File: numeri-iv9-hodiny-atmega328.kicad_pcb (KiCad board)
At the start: 2 copper layers, 160 x 50 mm, 64 parts, among them J2 Screw_Terminal_01x04, J3 USB-C, J4 PINHD_1x3_Female, J5 HW-084, Q1 BC557, Q2 BC557, SW1 RESET, SW2 Horizontal, SW3 Vertical, U1 ATmega328-P, U2 TPIC6B595N, U3 TPIC6B595N, U4 TPIC6B595N, U5 TPIC6B595N, Y1 6MHz

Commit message: preventívne
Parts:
- removed R17: 550R, Resistor_THT:R_Axial_DIN0207_L6.3mm_D2.5mm_P10.16mm_Horizontal
- added G***: LOGO, LOGO, F.Cu at (93.5, 75.8)
- added G***: LOGO, LOGO, F.Cu at (84.5, 93.2)
- added R4: 1K, Potentiometer_THT:Potentiometer_Bourns_3296W_Vertical, F.Cu at (200.0, 117.8)
- added REF**: JUP_P14mm, PCM_SL_Jumpers:JUP_P14mm, F.Cu at (211.8, 111.8)
- added REF**: JUP_P14mm, PCM_SL_Jumpers:JUP_P14mm, F.Cu at (130.2, 111.0)
- added REF**: JUP_P14mm, PCM_SL_Jumpers:JUP_P14mm, F.Cu at (157.8, 111.0)
- C12, C13, C14, C16, C3, C4, C5, C6, C7: footprint Capacitor_THT:C_Disc_D3.0mm_W2.0mm_P2.50mm -> Capacitor_THT:C_Disc_D6.0mm_W2.5mm_P5.00mm
- J4: footprint Connector_PinSocket_2.54mm:PinSocket_1x03_P2.54mm_Vertical -> Connector_PinHeader_2.54mm:PinHeader_1x03_P2.54mm_Vertical
- R1: footprint Resistor_THT:R_Axial_DIN0207_L6.3mm_D2.5mm_P10.16mm_Horizontal -> Resistor_THT:R_Axial_DIN0207_L6.3mm_D2.5mm_P5.08mm_Vertical; moved to B.Cu
- R11, R12, R6, R7, R9: footprint Resistor_THT:R_Axial_DIN0207_L6.3mm_D2.5mm_P10.16mm_Horizontal -> Resistor_THT:R_Axial_DIN0207_L6.3mm_D2.5mm_P15.24mm_Horizontal
- R13, R16: footprint Resistor_THT:R_Axial_DIN0207_L6.3mm_D2.5mm_P10.16mm_Horizontal -> Resistor_THT:R_Axial_DIN0207_L6.3mm_D2.5mm_P5.08mm_Vertical
- R15: footprint Resistor_THT:R_Axial_DIN0414_L11.9mm_D4.5mm_P15.24mm_Horizontal -> Resistor_THT:R_Axial_DIN0414_L11.9mm_D4.5mm_P25.40mm_Horizontal
- R8: footprint Resistor_THT:R_Axial_DIN0207_L6.3mm_D2.5mm_P2.54mm_Vertical -> Resistor_THT:R_Axial_DIN0207_L6.3mm_D2.5mm_P10.16mm_Horizontal
- SERIAL1: footprint Connector_PinHeader_2.54mm:PinHeader_1x02_P2.54mm_Vertical -> Connector_PinSocket_2.54mm:PinSocket_1x02_P2.54mm_Vertical
- SW2, SW3: footprint TerminalBlock_Phoenix:TerminalBlock_Phoenix_MPT-0,5-2-2.54_1x02_P2.54mm_Horizontal -> TerminalBlock_Phoenix:TerminalBlock_Phoenix_MPT-0,5-2-2.54_1x02_P2.54mm_Horizontal_RAW
- U2, U3, U4, U5: footprint Package_DIP:DIP-20_W7.62mm_Socket -> Package_DIP:DIP-20_W7.62mm_Socket_With_IC
- moved R5 65.2 mm to (125.7, 118.0), turned to 180 degrees
- moved D2 43.3 mm to (95.9, 103.2)
- moved R13 42.1 mm to (195.5, 117.8), turned to 90 degrees
- moved D1 28.1 mm to (161.7, 118.5), turned to 180 degrees
- moved R15 26.7 mm to (144.0, 99.4), turned to 90 degrees
- moved R16 22.4 mm to (189.8, 111.5), turned to 180 degrees
- moved Q2 20.0 mm to (187.0, 117.8), turned to 90 degrees
- moved C6 19.1 mm to (167.5, 84.1), turned to 90 degrees
- moved J4 19.1 mm to (115.5, 114.5), turned to -90 degrees
- moved TSV2 16.6 mm to (92.5, 92.2)
- moved TSV1 16.0 mm to (100.0, 92.5)
- moved RV2 12.1 mm to (90.2, 107.5)
- moved R14 11.8 mm to (172.7, 117.8)
- moved C7 9.29 mm to (149.5, 83.0)
- moved Q1 8.61 mm to (191.1, 115.2), turned to -90 degrees
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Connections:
- J4 pad 1: +3.3V -> +3V3
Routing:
- net +5V/+3V3: track 100.7 -> 9.05 mm
- net VBTN: track 13.7 -> 95.6 mm
- net +5V_DEC: track 28.8 -> 101.5 mm
- net MISO/HBTN: track 0.00 -> 66.4 mm
- net DEC_OUT: track 0.00 -> 34.6 mm
- net PB2: track 12.4 -> 43.0 mm
- net +3V3: track 0.00 -> 23.2 mm
- net +5V: track 169.7 -> 189.1 mm
- net ~{G}~: track 65.6 -> 47.5 mm
- net ~{PON}: track 9.34 -> 26.6 mm
- net Net-(U1-PC0): track 0.00 -> 9.25 mm
- net Net-(U1-XTAL2/PB7): track 8.24 -> 0.00 mm
- net Net-(U1-XTAL1/PB6): track 8.12 -> 0.00 mm
- net RX: track 0.00 -> 5.99 mm
- net Net-(Q2-E): track 0.00 -> 4.92 mm
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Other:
- board text added: "+5V VCC +3V3"

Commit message: preventívne
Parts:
- removed the REF** at (157.8, 111.0)
- added R10: 619R, Resistor_THT:R_Axial_DIN0207_L6.3mm_D2.5mm_P7.62mm_Horizontal, F.Cu at (248.2, 86.9)
- added R17: 464R, Resistor_THT:R_Axial_DIN0207_L6.3mm_D2.5mm_P2.54mm_Vertical, F.Cu at (192.0, 104.5)
- added R17: 464R, Resistor_THT:R_Axial_DIN0207_L6.3mm_D2.5mm_P2.54mm_Vertical, F.Cu at (198.0, 104.5)
- added R17: 464R, Resistor_THT:R_Axial_DIN0207_L6.3mm_D2.5mm_P2.54mm_Vertical, F.Cu at (195.0, 104.5)
- added R18: 464R, Resistor_THT:R_Axial_DIN0207_L6.3mm_D2.5mm_P7.62mm_Horizontal, B.Cu at (199.2, 96.2)
- added R19: 330R, Resistor_THT:R_Axial_DIN0207_L6.3mm_D2.5mm_P7.62mm_Horizontal, F.Cu at (245.8, 95.5)
- R16: footprint Resistor_THT:R_Axial_DIN0207_L6.3mm_D2.5mm_P5.08mm_Vertical -> Resistor_THT:R_Axial_DIN0207_L6.3mm_D2.5mm_P10.16mm_Horizontal
- moved R16 7.83 mm to (182.8, 115.0)
- moved RGB_LED1 4.78 mm to (186.5, 110.0)
- moved D1 2.09 mm to (163.3, 117.2)
- moved C12 0.72 mm to (182.5, 112.0)
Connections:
- RGB_LED1 pad 2: LED_R -> Net-(RGB_LED1-RA)
- RGB_LED1 pad 3: LED_G -> Net-(RGB_LED1-GA)
- RGB_LED1 pad 4: LED_B -> Net-(RGB_LED1-BA)
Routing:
- net PB2: track 43.0 -> 35.8 mm
- net LED_R: track 6.99 -> 0.16 mm
- net LED_G: track 6.99 -> 0.16 mm
- net LED_B: track 6.99 -> 0.16 mm
- net Net-(RGB_LED1-BA): track 0.00 -> 5.59 mm
- net Net-(Q1-B): track 0.00 -> 4.68 mm
- net unconnected-(U1-(PWM)PD5-Pad11): track 3.81 -> 7.19 mm
- net ~{PON}: track 26.6 -> 28.8 mm

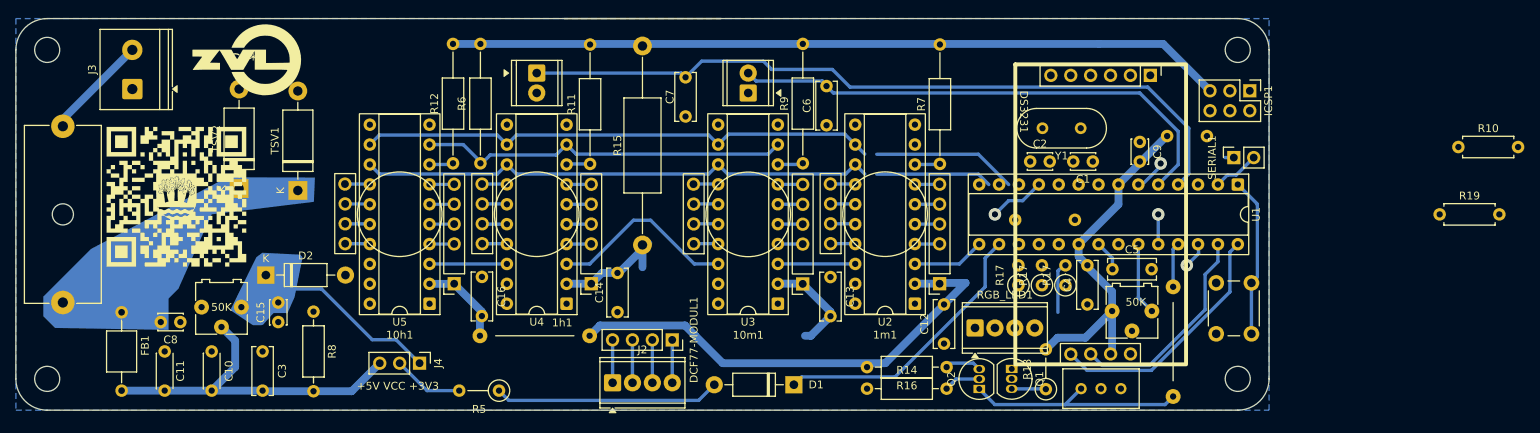
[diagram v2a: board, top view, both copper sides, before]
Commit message: Pridaná bloková schéma.
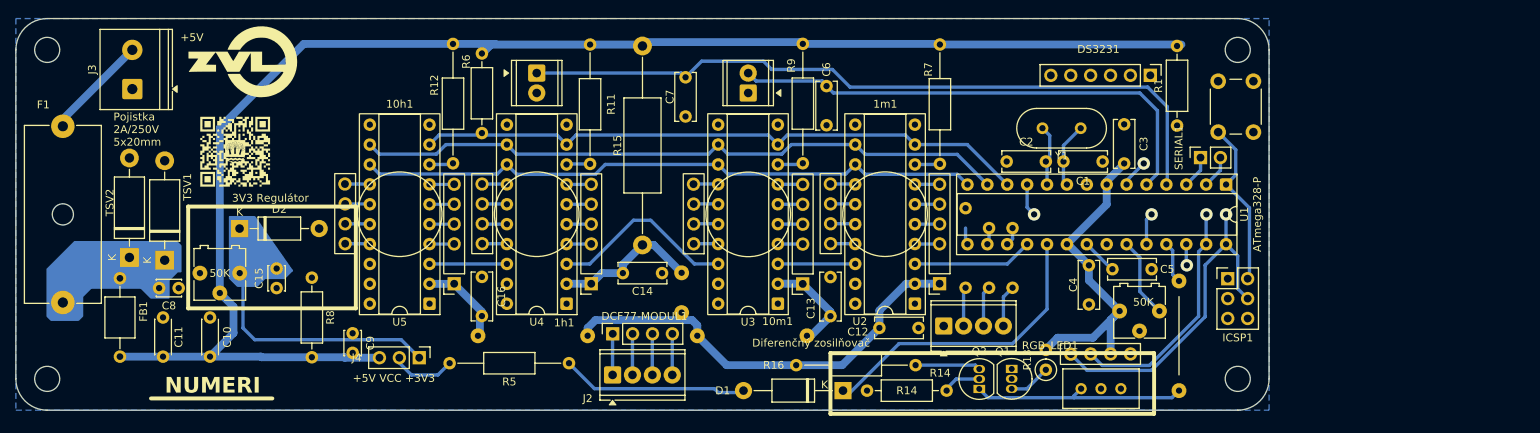
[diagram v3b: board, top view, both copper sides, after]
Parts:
- removed the R17 at (192.0, 104.5)
- removed the R17 at (198.0, 104.5)
- removed the R17 at (195.0, 104.5)
- removed R19: 330R, Resistor_THT:R_Axial_DIN0207_L6.3mm_D2.5mm_P7.62mm_Horizontal
- removed the REF** at (211.8, 111.8)
- added R17: 470R, Resistor_THT:R_Axial_DIN0207_L6.3mm_D2.5mm_P7.62mm_Horizontal, B.Cu at (188.2, 104.9)
- added REF**: JUP_P14mm, PCM_SL_Jumpers:JUP_P14mm, F.Cu at (212.5, 111.0)
- added REF**: JUP_P5.08mm, PCM_SL_Jumpers:JUP_P5.08mm, B.Cu at (149.0, 105.5)
- added REF**: JUP_P14mm, PCM_SL_Jumpers:JUP_P14mm, B.Cu at (158.0, 111.0)
- C1, C2: value 12p5 -> 68pF±5%; footprint Capacitor_THT:C_Disc_D3.0mm_W2.0mm_P2.50mm -> Capacitor_THT:C_Disc_D6.0mm_W2.5mm_P5.00mm
- D1: value 1N5822 -> SR260; footprint Diode_THT:D_DO-41_SOD81_P10.16mm_Horizontal -> Diode_THT:D_DO-41_SOD81_P12.70mm_Horizontal
- R1: footprint Resistor_THT:R_Axial_DIN0207_L6.3mm_D2.5mm_P5.08mm_Vertical -> Resistor_THT:R_Axial_DIN0207_L6.3mm_D2.5mm_P10.16mm_Horizontal; moved to F.Cu
- R10: value 619R -> 620R; footprint Resistor_THT:R_Axial_DIN0207_L6.3mm_D2.5mm_P7.62mm_Horizontal -> Resistor_THT:R_Axial_DIN0207_L6.3mm_D2.5mm_P10.16mm_Horizontal; moved to B.Cu
- R13: footprint Resistor_THT:R_Axial_DIN0207_L6.3mm_D2.5mm_P5.08mm_Vertical -> Resistor_THT:R_Axial_DIN0207_L6.3mm_D2.5mm_P2.54mm_Vertical
- R16: footprint Resistor_THT:R_Axial_DIN0207_L6.3mm_D2.5mm_P10.16mm_Horizontal -> Resistor_THT:R_Axial_DIN0207_L6.3mm_D2.5mm_P15.24mm_Horizontal
- R18: value 464R -> 470R
- R5: footprint Resistor_THT:R_Axial_DIN0207_L6.3mm_D2.5mm_P5.08mm_Vertical -> Resistor_THT:R_Axial_DIN0207_L6.3mm_D2.5mm_P15.24mm_Horizontal
- R6: footprint Resistor_THT:R_Axial_DIN0207_L6.3mm_D2.5mm_P15.24mm_Horizontal -> Resistor_THT:R_Axial_DIN0207_L6.3mm_D2.5mm_P10.16mm_Horizontal
- REF**: moved to B.Cu
- Y1: value 6MHz -> 16MHz±20ppm
- moved C3 113.8 mm to (205.5, 84.0)
- moved C9 103.4 mm to (107.0, 110.7)
- moved R10 65.4 mm to (185.2, 104.9), turned to 90 degrees
- moved SW1 32.6 mm to (222.0, 78.5), turned to -90 degrees
- moved ICSP1 24.1 mm to (218.7, 103.7), turned to 0 degrees
- moved TSV1 19.2 mm to (83.0, 101.3)
- moved TSV2 16.5 mm to (78.5, 101.0)
- moved R18 11.8 mm to (191.2, 104.9), turned to 90 degrees
- moved R5 9.60 mm to (134.6, 114.5)
- moved G*** 9.45 mm to (92.0, 87.5)
- moved DCF77-MODUL1 7.64 mm to (140.2, 110.8), turned to 90 degrees
- moved C14 7.56 mm to (146.5, 103.0), turned to 180 degrees
- moved D2 6.82 mm to (92.6, 97.3)
- moved D1 6.31 mm to (169.6, 118.0)
- moved C10 4.35 mm to (88.8, 108.7)
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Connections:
- C6 pad 2: MISO/HBTN -> HBTN
- D1 pad 1: PB2 -> PB5
- ICSP1 pad 3: MOSI/SRCK -> LED_B/MOSI
- ICSP1 pad 6: MISO/HBTN -> SER_IN/MISO
- R18 pad 2: LED_B -> LED_B/MOSI
- SW2 pad 2: MISO/HBTN -> HBTN
- U1 pad 14: MOSI/SRCK -> SRCK
- U1 pad 15: SER_IN -> LED_R
- U1 pad 16: PB2 -> LED_G
- U1 pad 17: LED_R -> LED_B/MOSI
- U1 pad 18: LED_G -> SER_IN/MISO
- U1 pad 19: LED_B -> PB5
- U1 pad 5: MISO/HBTN -> HBTN
- U2 pad 13: MOSI/SRCK -> SRCK
- U2 pad 3: SER_IN -> SER_IN/MISO
- U3 pad 13: MOSI/SRCK -> SRCK
- U4 pad 13: MOSI/SRCK -> SRCK
- U5 pad 13: MOSI/SRCK -> SRCK
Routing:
- net MOSI/SRCK: track 81.6 -> 0.00 mm
- net SRCK: track 0.00 -> 80.4 mm
- net MISO/HBTN: track 66.4 -> 0.00 mm
- net HBTN: track 0.00 -> 64.8 mm
- net +5V: track 189.1 -> 238.5 mm
- net PB5: track 0.00 -> 38.8 mm
- net PB2: track 35.8 -> 0.00 mm
- net ~{G}~: track 47.5 -> 78.9 mm
- net SER_IN/MISO: track 0.00 -> 15.4 mm
- net +3V3: track 23.2 -> 34.8 mm
- net SCL: track 32.0 -> 43.2 mm, vias 0 -> 1
- net SER_IN: track 9.25 -> 0.00 mm
- net Net-(U1-XTAL1/PB6): track 0.00 -> 8.28 mm
- net Net-(U1-XTAL2/PB7): track 0.00 -> 7.72 mm
- net Net-(RGB_LED1-GA): track 0.00 -> 5.17 mm
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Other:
- board text added: "+5V"
- board text added: "3V3 Regulátor"
- board text added: "Diferenčný zosilňovač"
- board text added: "NUMERI"
- board text added: "Pojistka 2A/250V 5x20mm"

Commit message: preventivne
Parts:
- removed ICSP1: 2x3, Connector_PinHeader_2.54mm:PinHeader_2x03_P2.54mm_Vertical
- removed J2: Screw_Terminal_01x04, TerminalBlock_Phoenix:TerminalBlock_Phoenix_MPT-0,5-4-2.54_1x04_P2.54mm_Horizontal
- removed R5: 10K, Resistor_THT:R_Axial_DIN0207_L6.3mm_D2.5mm_P15.24mm_Horizontal
- removed R6: 10K, Resistor_THT:R_Axial_DIN0207_L6.3mm_D2.5mm_P10.16mm_Horizontal
- removed the REF** at (212.5, 111.0)
- removed the REF** at (130.0, 111.0)
- removed the REF** at (149.0, 105.5)
- removed the REF** at (158.0, 111.0)
- removed SERIAL1: 1x2, Connector_PinSocket_2.54mm:PinSocket_1x02_P2.54mm_Vertical
- added C17: 100nF, Capacitor_THT:C_Disc_D6.0mm_W2.5mm_P5.00mm, F.Cu at (123.6, 103.5)
- added D4: 1N4148, Diode_THT:D_DO-35_SOD27_P7.62mm_Horizontal, F.Cu at (208.7, 85.0)
- added J6: 2x3, Connector_PinHeader_2.54mm:PinHeader_2x03_P2.54mm_Vertical, F.Cu at (218.2, 103.9)
- added J7: 1x2, Connector_PinSocket_2.54mm:PinSocket_1x02_P2.54mm_Vertical, F.Cu at (215.2, 88.2)
- added R19: 27R, Resistor_THT:R_Axial_DIN0207_L6.3mm_D2.5mm_P10.16mm_Horizontal, F.Cu at (100.0, 103.5)
- added R2: 620R, Resistor_THT:R_Axial_DIN0207_L6.3mm_D2.5mm_P7.62mm_Horizontal, B.Cu at (184.8, 103.6)
- added R3: 470R, Resistor_THT:R_Axial_DIN0207_L6.3mm_D2.5mm_P7.62mm_Horizontal, B.Cu at (187.8, 103.6)
- added RV3: 1K, Potentiometer_THT:Potentiometer_Bourns_3296W_Vertical, F.Cu at (176.1, 116.0)
- C10: footprint Capacitor_THT:C_Disc_D4.3mm_W1.9mm_P5.00mm -> Capacitor_THT:C_Disc_D6.0mm_W2.5mm_P5.00mm
- C11: value 4u7 -> 100nF; footprint Capacitor_THT:C_Disc_D4.3mm_W1.9mm_P5.00mm -> Capacitor_THT:C_Disc_D6.0mm_W2.5mm_P5.00mm
- C12: value 100nF -> 4u7
- C15: value 1uF -> 100nF; footprint Capacitor_THT:C_Disc_D3.0mm_W2.0mm_P2.50mm -> Capacitor_THT:C_Disc_D6.0mm_W2.5mm_P5.00mm
- C16: value 100nF -> 1uF
- C8, C9: footprint Capacitor_THT:C_Disc_D3.0mm_W2.0mm_P2.50mm -> Capacitor_THT:C_Disc_D6.0mm_W2.5mm_P5.00mm
- D1: value SR260 -> 1N5819
- D2: footprint Diode_THT:D_DO-41_SOD81_P10.16mm_Horizontal -> Diode_THT:D_DO-35_SOD27_P7.62mm_Horizontal
- R1, R8: footprint Resistor_THT:R_Axial_DIN0207_L6.3mm_D2.5mm_P10.16mm_Horizontal -> Resistor_THT:R_Axial_DIN0207_L6.3mm_D2.5mm_P7.62mm_Horizontal
- R10: value 620R -> 10K; moved to F.Cu
- R11, R12, R9: footprint Resistor_THT:R_Axial_DIN0207_L6.3mm_D2.5mm_P15.24mm_Horizontal -> Resistor_THT:R_Axial_DIN0207_L6.3mm_D2.5mm_P7.62mm_Horizontal
- R13: footprint Resistor_THT:R_Axial_DIN0207_L6.3mm_D2.5mm_P2.54mm_Vertical -> Resistor_THT:R_Axial_DIN0207_L6.3mm_D2.5mm_P15.24mm_Horizontal
- R15: value 1R±5% -> 10K; footprint Resistor_THT:R_Axial_DIN0414_L11.9mm_D4.5mm_P25.40mm_Horizontal -> Resistor_THT:R_Axial_DIN0207_L6.3mm_D2.5mm_P7.62mm_Horizontal
- R16: value 20R -> 1R±5%; footprint Resistor_THT:R_Axial_DIN0207_L6.3mm_D2.5mm_P15.24mm_Horizontal -> Resistor_THT:R_Axial_DIN0414_L11.9mm_D4.5mm_P20.32mm_Horizontal
- R17: value 470R -> 20R; footprint Resistor_THT:R_Axial_DIN0207_L6.3mm_D2.5mm_P7.62mm_Horizontal -> Resistor_THT:R_Axial_DIN0207_L6.3mm_D2.5mm_P10.16mm_Horizontal; moved to F.Cu
- R18: value 470R -> 330R; moved to F.Cu
- R4: value 1K -> 470R; footprint Potentiometer_THT:Potentiometer_Bourns_3296W_Vertical -> Resistor_THT:R_Axial_DIN0207_L6.3mm_D2.5mm_P7.62mm_Horizontal; moved to B.Cu
- RGB_LED1: footprint TerminalBlock_Phoenix:TerminalBlock_Phoenix_MPT-0,5-4-2.54_1x04_P2.54mm_Horizontal -> Connector_JST:JST_XH_B4B-XH-A_1x04_P2.50mm_Vertical
- RV2: value 50K -> 10K
- SW2, SW3: footprint TerminalBlock_Phoenix:TerminalBlock_Phoenix_MPT-0,5-2-2.54_1x02_P2.54mm_Horizontal_RAW -> TerminalBlock_Phoenix:TerminalBlock_Phoenix_PT-1,5-2-5.0-H_1x02_P5.00mm_Horizontal
- moved C11 139.2 mm to (219.0, 80.1)
- moved R8 87.2 mm to (187.8, 89.1), turned to 90 degrees
- moved C12 84.3 mm to (95.0, 108.7), turned to -90 degrees
- moved R10 79.8 mm to (105.5, 103.5), turned to -90 degrees
- moved R7 52.8 mm to (135.1, 113.5), turned to 180 degrees
- moved C15 49.2 mm to (146.5, 105.0), turned to 180 degrees
- moved D1 47.0 mm to (122.7, 117.0), turned to 0 degrees
- moved R1 45.7 mm to (167.8, 73.8), turned to -90 degrees
- moved SW1 42.8 mm to (179.2, 77.8), turned to 180 degrees
- moved R16 37.2 mm to (144.0, 101.7), turned to 90 degrees
- moved R18 32.8 mm to (215.0, 82.3)
- moved R17 27.8 mm to (162.2, 114.5), turned to 180 degrees
- moved C6 27.6 mm to (140.5, 78.5)
- moved R11 27.2 mm to (164.5, 89.0)
- moved SW2 26.2 mm to (132.1, 73.5), turned to -90 degrees
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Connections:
- net /H1_2 renamed /Hlavná Schéma/H1_2
- net /H1_3 renamed /Hlavná Schéma/H1_3
- net /H1_4 renamed /Hlavná Schéma/H1_4
- net /H1_5 renamed /Hlavná Schéma/H1_5
- net /H1_6 renamed /Hlavná Schéma/H1_6
- net /H1_7 renamed /Hlavná Schéma/H1_7
- net /H1_8 renamed /Hlavná Schéma/H1_8
- net /H1_9 renamed /Hlavná Schéma/H1_9
- net /H2_2 renamed /Hlavná Schéma/H2_2
- net /H2_3 renamed /Hlavná Schéma/H2_3
- net /H2_4 renamed /Hlavná Schéma/H2_4
- net /H2_5 renamed /Hlavná Schéma/H2_5
- net /H2_6 renamed /Hlavná Schéma/H2_6
- net /H2_7 renamed /Hlavná Schéma/H2_7
- net /H2_8 renamed /Hlavná Schéma/H2_8
- net /H2_9 renamed /Hlavná Schéma/H2_9
- net /M1_2 renamed /Hlavná Schéma/M1_2
- net /M1_3 renamed /Hlavná Schéma/M1_3
- net /M1_4 renamed /Hlavná Schéma/M1_4
- net /M1_5 renamed /Hlavná Schéma/M1_5
- net /M1_6 renamed /Hlavná Schéma/M1_6
- net /M1_7 renamed /Hlavná Schéma/M1_7
- net /M1_8 renamed /Hlavná Schéma/M1_8
- net /M1_9 renamed /Hlavná Schéma/M1_9
- net /M2_2 renamed /Hlavná Schéma/M2_2
- net /M2_3 renamed /Hlavná Schéma/M2_3
- net /M2_4 renamed /Hlavná Schéma/M2_4
- net /M2_5 renamed /Hlavná Schéma/M2_5
- net /M2_6 renamed /Hlavná Schéma/M2_6
- net /M2_7 renamed /Hlavná Schéma/M2_7
- net /M2_8 renamed /Hlavná Schéma/M2_8
- net /M2_9 renamed /Hlavná Schéma/M2_9
- net Net-(TSV1-A1) renamed VBUS_FUSED
- C11 pad 2: +5V -> ~{RESET}
- C12 pad 2: +5V_DEC -> +5V
- C15 pad 2: +3V3 -> +5V_DEC
- C16 pad 2: +5V_DEC -> +3V3
- R1 pad 1: ~{RESET} -> Net-(R1-Pad1)
- R10 pad 1: Net-(RGB_LED1-RA) -> GND
- R10 pad 2: LED_R -> +5V
- R11 pad 1: Net-(U4-~{SRCLR}) -> Net-(U3-~{SRCLR})
- R12 pad 1: Net-(U5-~{SRCLR}) -> Net-(U4-~{SRCLR})
- R15 pad 1: +5V_DEC -> Net-(U5-~{SRCLR})
- R16 pad 1: Net-(Q2-E) -> +5V_DEC
- R16 pad 2: +5V_DEC -> +5V
- R17 pad 1: Net-(RGB_LED1-GA) -> Net-(Q2-E)
- R17 pad 2: LED_G -> +5V_DEC
- R18 pad 1: Net-(RGB_LED1-BA) -> ~{RESET}
- R18 pad 2: LED_B/MOSI -> Net-(R1-Pad1)
- R4 pad 1: DEC_OUT -> Net-(RGB_LED1-BA)
- R4 pad 2: GND -> LED_B/MOSI
- R7 pad 1: Net-(U2-~{SRCLR}) -> ~{PON}
- R7 pad 2: +5V -> +5V/+3V3
- R8 pad 1: GND -> ~{G}~
- R9 pad 1: Net-(U3-~{SRCLR}) -> Net-(U2-~{SRCLR})
- RV1 pad 1: GND -> Net-(U1-PC0)
- RV2 pad 1: +5V -> +3V3
- RV2 pad 3: GND -> Net-(R19-Pad1)
- SW1 pad 2: ~{RESET} -> Net-(R1-Pad1)
- SW3 pad 1: VBTN -> GND
- SW3 pad 2: GND -> VBTN
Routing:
- net SER_IN/MISO: track 15.4 -> 74.0 mm
- net LED_B/MOSI: track 2.34 -> 59.8 mm
- net Net-(R1-Pad1): track 0.00 -> 48.1 mm
- net +5V_DEC: track 99.4 -> 63.6 mm, vias 0 -> 4
- net HBTN: track 64.8 -> 100.2 mm
- net PB5: track 38.8 -> 6.73 mm, vias 0 -> 1
- net Net-(Q1-E): track 5.37 -> 27.6 mm
- net ~{PON}: track 23.8 -> 3.60 mm
- net DEC_OUT: track 33.2 -> 14.1 mm, vias 0 -> 1
- net VBTN: track 94.0 -> 81.2 mm
- net +5V: track 238.5 -> 231.5 mm
- net Net-(Q1-B): track 4.68 -> 10.4 mm
- net ~{RESET}: track 21.5 -> 26.9 mm
- net Net-(RGB_LED1-RA): track 4.98 -> 10.4 mm
- net Net-(J2-Pin_3): track 4.99 -> 0.00 mm
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- added copper zone on B.Cu, net +3V3
- added copper zone on B.Cu, net VBUS_FUSED
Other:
- board text removed: "Diferenčný zosilňovač"
- board text removed: "NUMERI"

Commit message: Prvá iterácia.
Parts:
- added C18: 4u7, Capacitor_THT:C_Disc_D6.0mm_W2.5mm_P5.00mm, F.Cu at (147.2, 109.2)
- added C19: 1uF, Capacitor_THT:C_Disc_D6.0mm_W2.5mm_P5.00mm, F.Cu at (211.5, 109.0)
- added J2: Screw_Terminal_01x04, Connector_PinSocket_2.54mm:PinSocket_1x04_P2.54mm_Vertical, F.Cu at (140.2, 117.5)
- added Q3: BC547, Package_TO_SOT_THT:TO-92_Inline, F.Cu at (176.5, 111.3)
- added R20: 10R, Resistor_THT:R_Axial_DIN0207_L6.3mm_D2.5mm_P7.62mm_Horizontal, F.Cu at (214.2, 82.8)
- added R23: 10K, Resistor_THT:R_Axial_DIN0207_L6.3mm_D2.5mm_P10.16mm_Horizontal, F.Cu at (105.0, 103.5)
- added REF**: OSHW-Symbol_6.7x6mm_SilkScreen, Symbol:OSHW-Symbol_6.7x6mm_SilkScreen, F.Cu at (186.6, 74.8)
- added REF**: WEEE-Logo_4.2x6mm_SilkScreen, Symbol:WEEE-Logo_4.2x6mm_SilkScreen, F.Cu at (75.6, 112.0)
- F1: value F1A25 -> F1A25/F900mA
- R10: value 10K -> 620R; footprint Resistor_THT:R_Axial_DIN0207_L6.3mm_D2.5mm_P10.16mm_Horizontal -> Resistor_THT:R_Axial_DIN0207_L6.3mm_D2.5mm_P7.62mm_Horizontal
- R17: value 20R -> 27R
- Y1: value 16MHz±20ppm -> 16MHz±30ppm
- moved R10 60.7 mm to (165.7, 111.5), turned to 0 degrees
- moved R18 8.61 mm to (214.1, 73.8), turned to 180 degrees
- moved C15 7.15 mm to (140.8, 109.2), turned to 90 degrees
- moved R14 3.49 mm to (152.1, 114.0)
- moved R17 2.71 mm to (162.3, 117.2)
- moved DCF77-MODUL1 1.72 mm to (140.2, 113.2)
- moved D4 1.56 mm to (208.8, 83.4), turned to 45 degrees
- moved C11 1.54 mm to (220.5, 79.8)
- moved RV1 1.06 mm to (206.4, 108.0)
- moved G*** 0.50 mm to (91.6, 87.2)
- moved C6 0.25 mm to (140.8, 78.5)
- moved C7 0.25 mm to (147.2, 78.5)
- moved C5 0.20 mm to (203.8, 102.5)
- moved SW1 0.15 mm to (179.2, 77.9)
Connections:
- Q1 pad 1: Net-(Q1-B) -> Net-(Q1-C)
- R10 pad 1: GND -> DEC_ENA
- R10 pad 2: +5V -> Net-(Q3-B)
- R14 pad 2: Net-(Q1-B) -> Net-(Q1-C)
- U1 pad 24: unconnected-(U1-PC1-Pad24) -> DEC_ENA
- U1 pad 6: unconnected-(U1-PD4-Pad6) -> Net-(U1-PD4)
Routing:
- net Net-(Q1-C): track 0.00 -> 24.1 mm
- net ~{RESET}: track 26.9 -> 37.5 mm
- net Net-(R1-Pad1): track 48.1 -> 39.1 mm
- net Net-(Q3-B): track 0.00 -> 6.00 mm
- net Net-(U1-PD4): track 0.00 -> 5.24 mm
- net Net-(J2-Pin_3): track 0.00 -> 4.75 mm
- net Net-(J2-Pin_2): track 0.00 -> 4.75 mm
- net Net-(J2-Pin_1): track 0.00 -> 4.75 mm
- net Net-(J2-Pin_4): track 0.00 -> 4.25 mm
- net unconnected-(U1-PC1-Pad24): track 4.08 -> 0.00 mm, vias 1 -> 0
- net DEC_ENA: track 0.00 -> 4.08 mm, vias 0 -> 1
- net unconnected-(U1-PD4-Pad6): track 3.60 -> 0.00 mm, vias 1 -> 0
- net +5V_DEC: track 63.6 -> 66.3 mm
- net +5V: track 231.5 -> 233.9 mm
- net DEC_OUT: track 14.1 -> 16.1 mm
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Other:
- board text added: "2025"
- board text added: "Batéria: CR2032"
- board text added: "DCF77-MODUL"
- board text added: "HW-084"
- board text added: "Hod 1"
- board text added: "Hod 10"
- board text added: "ICSP"
- board text added: "Manuál"
- board text added: "Min 1"
- board text added: "Min 10"
- board text added: "Nastavovanie napájacieho napätia pre DCF77 príjimač"
- board text added: "Podržaním vymažete EEPROM"
- board text added: "RESET"
- board text added: "RX"
- board text added: "Senzorový rezistor 1Ω ± 5%"
- board text added: "TX"
